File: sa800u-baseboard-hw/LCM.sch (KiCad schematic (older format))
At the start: 2 parts

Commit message: added chokes on datalines
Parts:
- removed J?: 1-1734248-5, antmicro-footprints:TE_1-1734248-5, symbol antmicroFCCConnectors:1-1734248-5
- added L? (x8): 744235900, antmicro-footprints:744235900, symbol antmicroFixedInductors:744235900
- added U3: FFC-1mm-30pin, symbol Connectors:FFC-1mm-30pin
- gave numbers to parts that had none: 1
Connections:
- wire segments 49 -> 97
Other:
- note added: "TODO: I2C needs pullups"
- moved on the sheet: J2

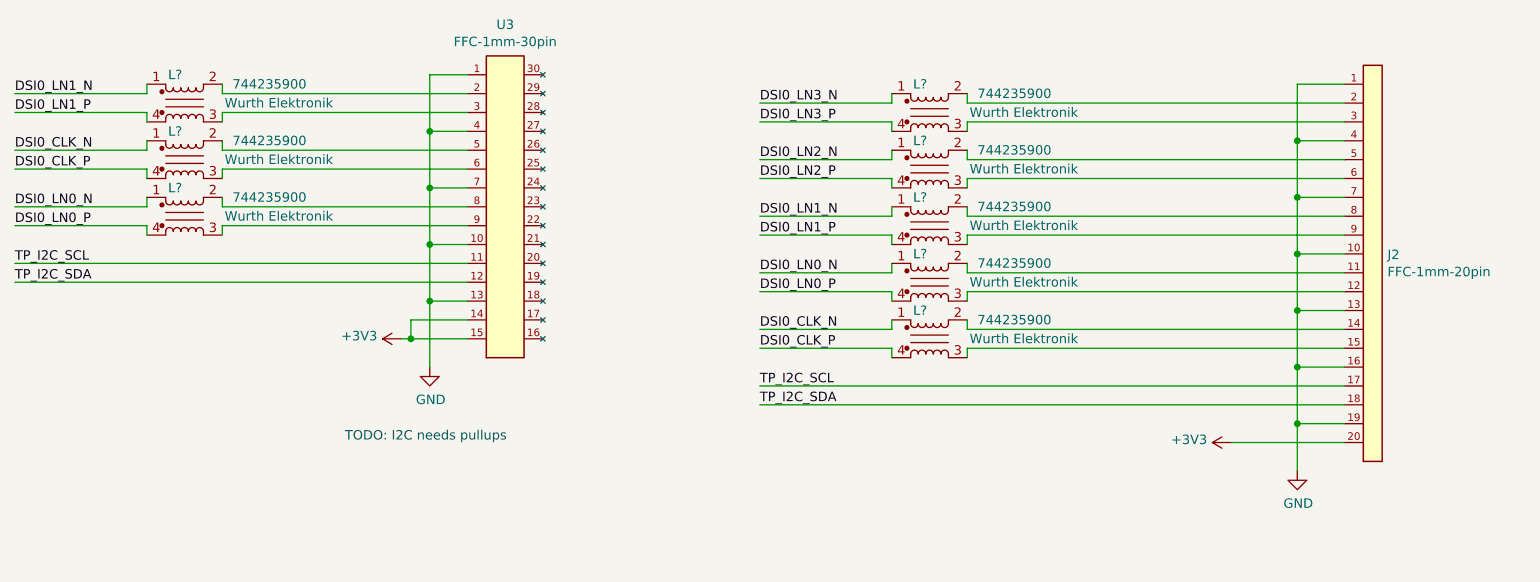
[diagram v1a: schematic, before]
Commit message: added HDMI converter
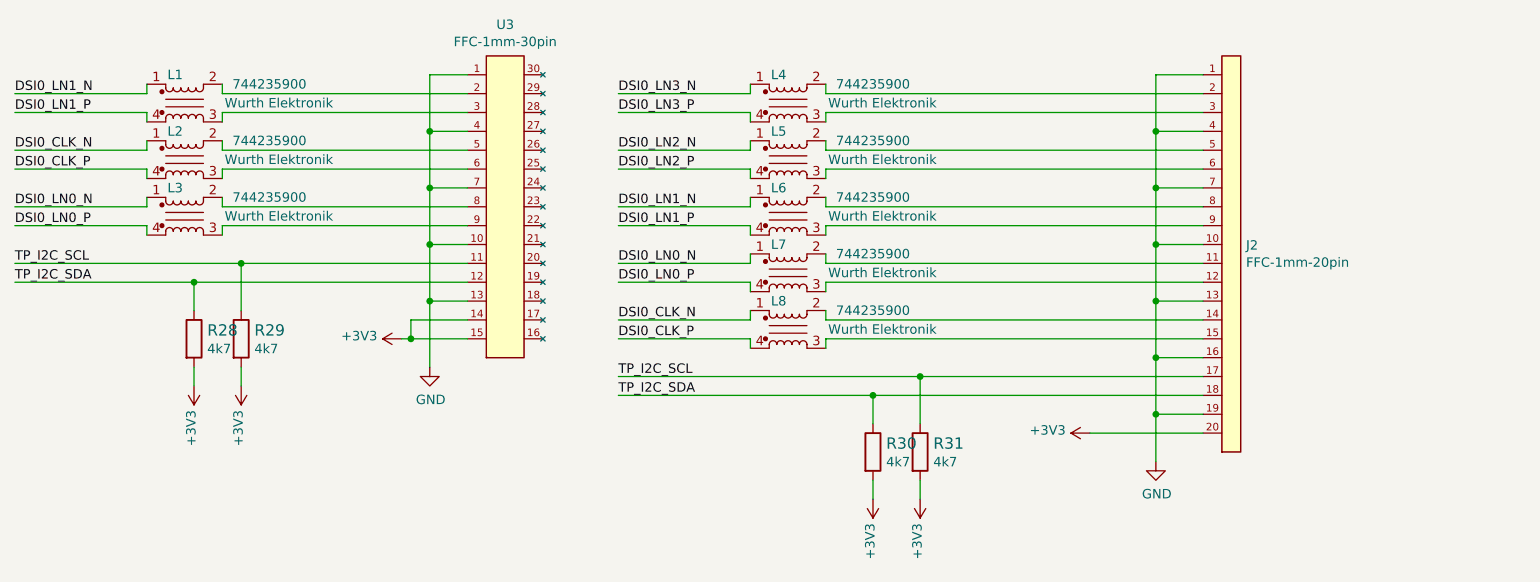
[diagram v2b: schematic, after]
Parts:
- added R28, R29, R30, R31: R_4k7_0402, antmicro-footprints:0402-res, symbol antmicroResistors0402:R_4k7_0402
- gave numbers to parts that had none: 8
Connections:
- net +3V3: now also R28.2, R29.2, R30.2, R31.2
- net TP_I2C_SCL: now also R29.1, R31.1
- net TP_I2C_SDA: now also R28.1, R30.1
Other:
- note removed: "TODO: I2C needs pullups"
- moved on the sheet: J2, L4, L5, L6, L7, L8
